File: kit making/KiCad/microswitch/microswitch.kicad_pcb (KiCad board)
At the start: 2 copper layers, 35 x 17 mm, 2 parts, among them J1 Conn_01x03_Pin, J2 Conn_01x03_Pin

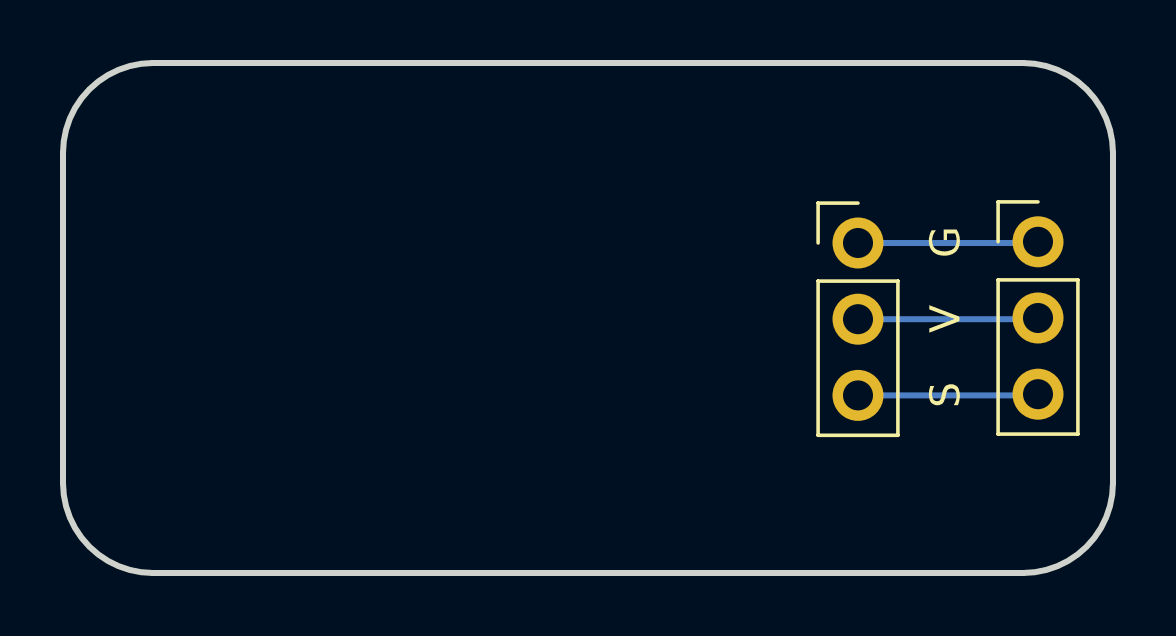
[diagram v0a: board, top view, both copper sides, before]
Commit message: Worksheet updates, box inserts, updated controller code
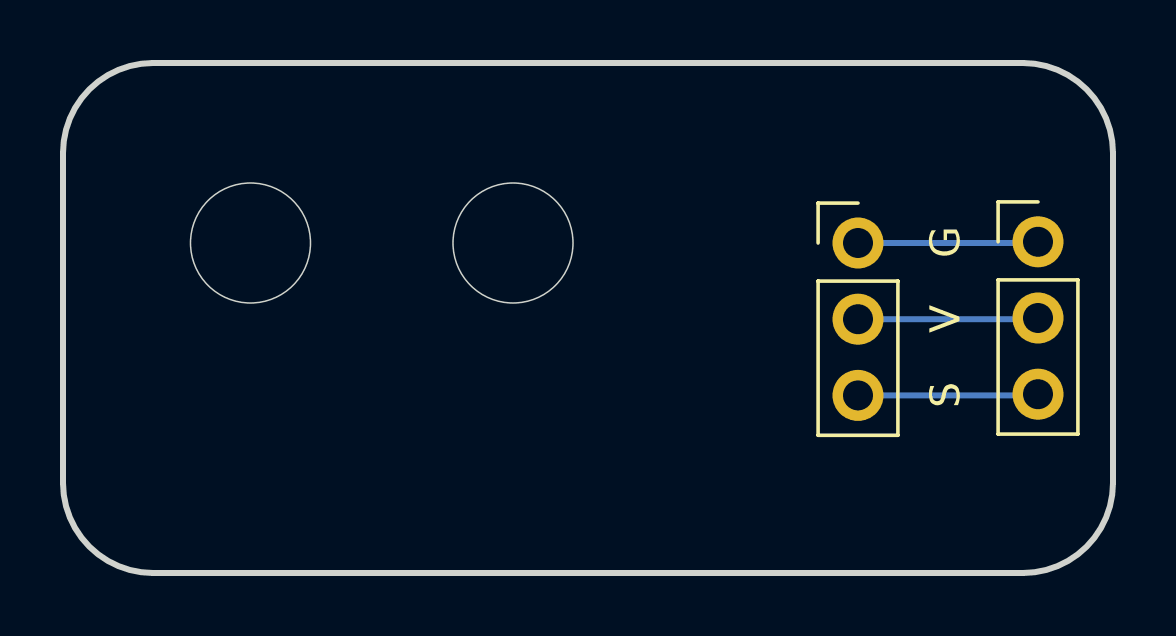
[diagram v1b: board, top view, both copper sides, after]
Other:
- outline, holes or cut-outs redrawn
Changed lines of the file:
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@@
 		)
 		(property "Value" "Conn_01x03_Pin"
-			(at 0 7.41 360)
+			(at 0 7.41 0)
 			(layer "F.Fab")
 			(effects
@@
 		(layer "Edge.Cuts")
 	)
+	(gr_circle
+		(center 103.25 53)
+		(end 103.25 51)
+		(stroke
+			(width 0.05)
+			(type default)
+		)
+		(fill none)
+		(layer "Edge.Cuts")
+	)
 	(gr_arc
 		(start 97 50)
@@
 		(layer "Edge.Cuts")
 	)
+	(gr_circle
+		(center 112 53)
+		(end 112 51)
+		(stroke
+			(width 0.05)
+			(type default)
+		)
+		(fill none)
+		(layer "Edge.Cuts")
+	)
 	(gr_text "G"
-		(at 127 57.5 90)
-		(layer "B.SilkS")
-		(effects
-			(font
-				(size 1 1)
-				(thickness 0.1)
-			)
-			(justify left bottom mirror)
-		)
-	)
-	(gr_text "V"
-		(at 127 55 90)
-		(layer "B.SilkS")
-		(effects
-			(font
-				(size 1 1)
-				(thickness 0.1)
-			)
-			(justify left bottom mirror)
-		)
-	)
-	(gr_text "S"
-		(at 127 52.5 90)
-		(layer "B.SilkS")
-		(effects
-			(font
-				(size 1 1)
-				(thickness 0.1)
-			)
-			(justify left bottom mirror)
-		)
-	)
-	(gr_text "G"
